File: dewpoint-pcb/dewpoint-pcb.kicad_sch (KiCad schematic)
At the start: 15 parts, among them J1 Power Terminal, J2 Relais Connector, J3 Sensor Outside, J4 Sensor Inside, J5 Display Connector, J6 Reset Button, J7 3-way On/Auto/Off-Switch

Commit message: v1.0, gerber.zip
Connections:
- net GND: now also J2.1 (Pin_1); no longer J2.3 (Pin_3)
- net Relais: now also J2.3 (Pin_3); no longer J2.1 (Pin_1)
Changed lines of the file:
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@@
     )
   )
-  (global_label "Relais" (shape input) (at 91.44 68.58 0) (fields_autoplaced)
+  (global_label "Relais" (shape input) (at 91.44 63.5 0) (fields_autoplaced)
     (effects (font (size 1.27 1.27)) (justify left))
-    (property "Intersheet References" "${INTERSHEET_REFS}" (id 0) (at 99.6588 68.6594 0)
+    (property "Intersheet References" "${INTERSHEET_REFS}" (id 0) (at 99.6588 63.5794 0)
       (effects (font (size 1.27 1.27)) (justify left) hide)
     )
@@
     (pin "1")
   )
-  (symbol (lib_id "power:GND") (at 91.44 63.5 90) (unit 1)
-    (in_bom yes) (on_board yes) (fields_autoplaced)
-    (property "Reference" "#PWR01" (id 0) (at 97.79 63.5 0)
-      (effects (font (size 1.27 1.27)) hide)
-    )
-    (property "Value" "GND" (id 1) (at 95.25 63.4999 90)
-      (effects (font (size 1.27 1.27)) (justify right))
-    )
-    (property "Footprint" "" (id 2) (at 91.44 63.5 0)
-      (effects (font (size 1.27 1.27)) hide)
-    )
-    (property "Datasheet" "" (id 3) (at 91.44 63.5 0)
-      (effects (font (size 1.27 1.27)) hide)
-    )
+  (symbol (lib_id "power:GND") (at 91.44 68.58 90) (unit 1)
+    (in_bom yes) (on_board yes) (fields_autoplaced)
+    (property "Reference" "#PWR01" (id 0) (at 97.79 68.58 0)
+      (effects (font (size 1.27 1.27)) hide)
+    )
+    (property "Value" "GND" (id 1) (at 95.25 68.5799 90)
+      (effects (font (size 1.27 1.27)) (justify right))
+    )
+    (property "Footprint" "" (id 2) (at 91.44 68.58 0)
+      (effects (font (size 1.27 1.27)) hide)
+    )
+    (property "Datasheet" "" (id 3) (at 91.44 68.58 0)
+      (effects (font (size 1.27 1.27)) hide)
+    )

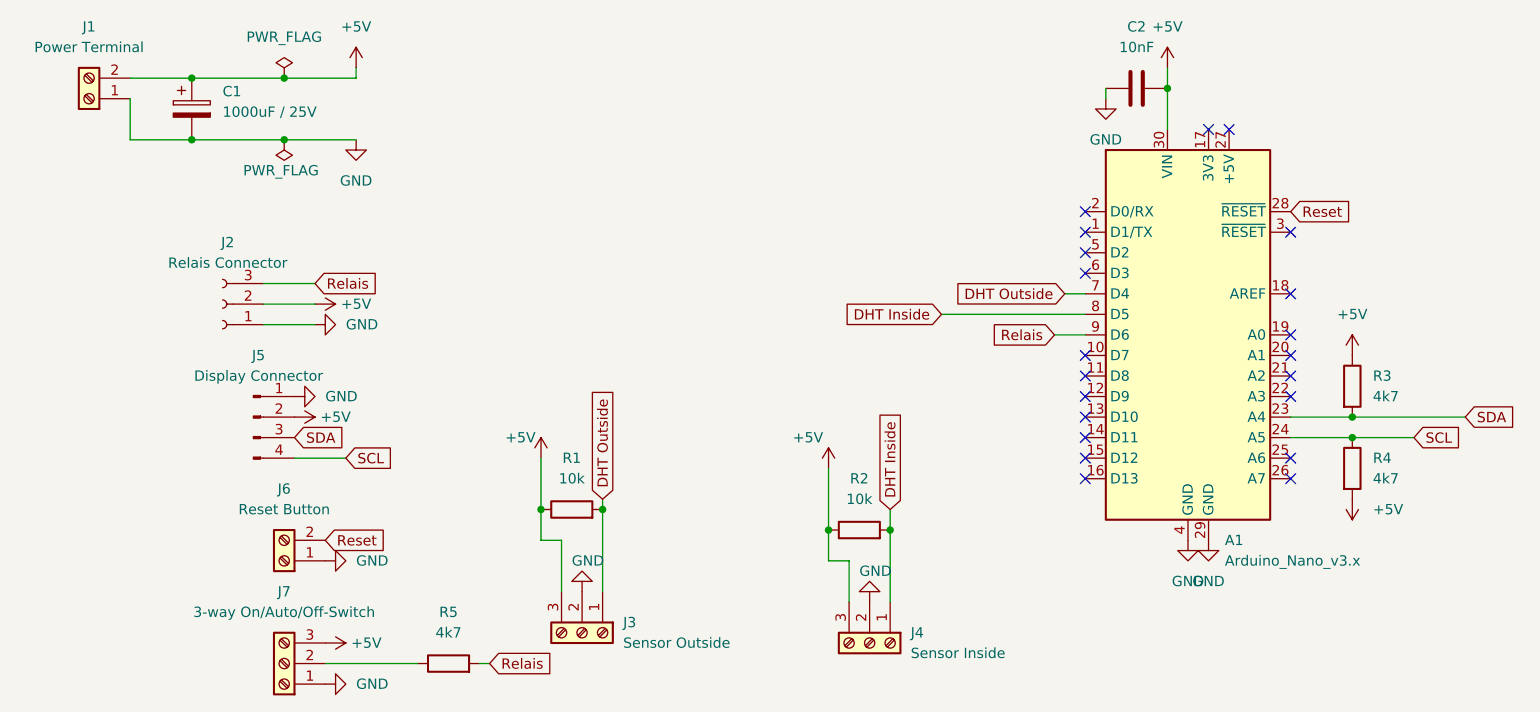
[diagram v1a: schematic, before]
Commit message: Correction, Relais switch wasn't connected correctly.
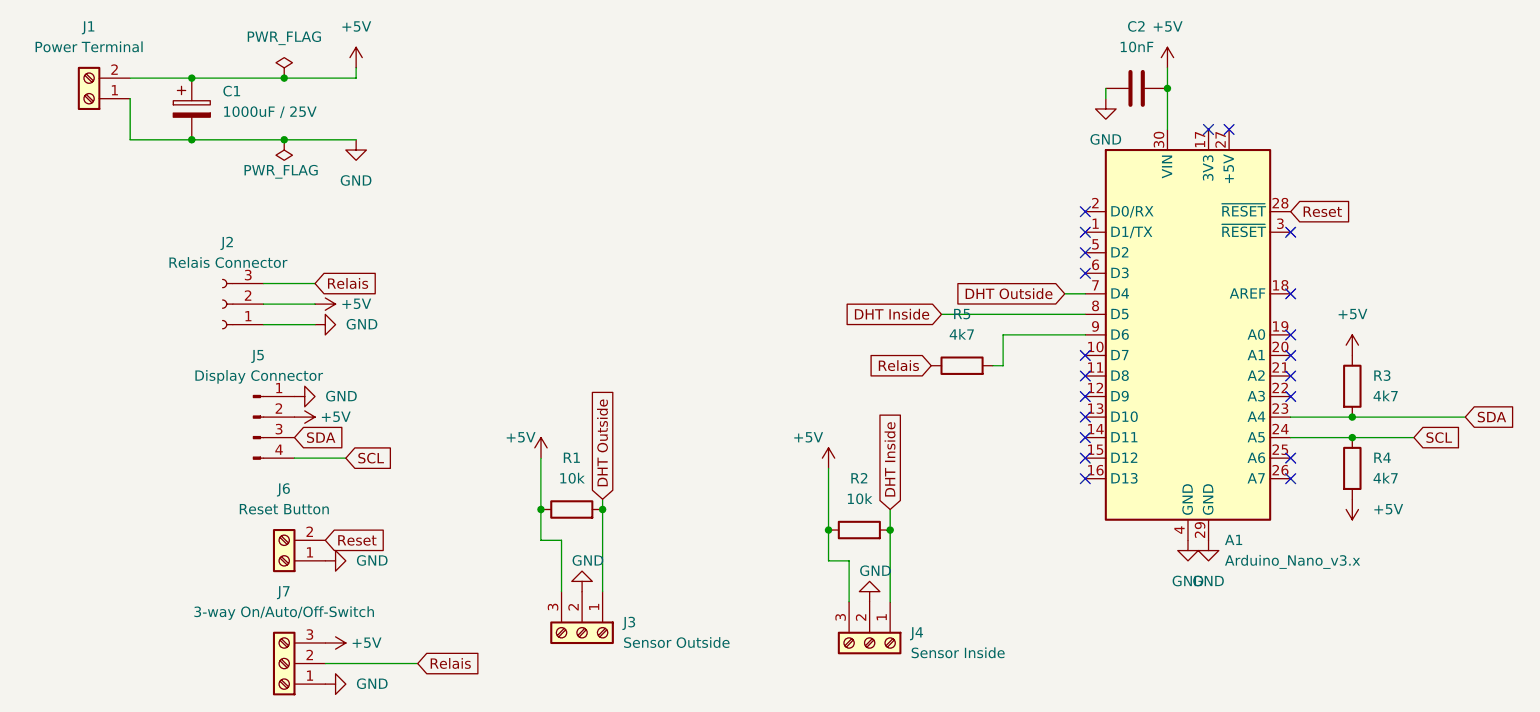
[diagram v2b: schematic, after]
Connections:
- net Relais: now also J7.2 (Pin_2), R5.1; no longer A1.9 (D6), R5.2
- new net: A1.9 (D6), R5.2
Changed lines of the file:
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@@
     (stroke (width 0) (type default) (color 0 0 0 0))
   )
-  (wire (pts (xy 182.88 69.85) (xy 186.69 69.85))
+  (wire (pts (xy 176.53 69.85) (xy 186.69 69.85))
     (stroke (width 0) (type default) (color 0 0 0 0))
   )
@@
     (stroke (width 0) (type default) (color 0 0 0 0))
   )
+  (wire (pts (xy 176.53 73.66) (xy 175.26 73.66))
+    (stroke (width 0) (type default) (color 0 0 0 0))
+  )
   (wire (pts (xy 212.09 82.55) (xy 219.71 82.55))
     (stroke (width 0) (type default) (color 0 0 0 0))
   )
-  (wire (pts (xy 111.76 110.49) (xy 113.03 110.49))
+  (wire (pts (xy 176.53 69.85) (xy 176.53 73.66))
     (stroke (width 0) (type default) (color 0 0 0 0))
   )
@@
     )
   )
-  (global_label "Relais" (shape input) (at 182.88 69.85 180) (fields_autoplaced)
+  (global_label "Relais" (shape input) (at 167.64 73.66 180) (fields_autoplaced)
     (effects (font (size 1.27 1.27)) (justify right))
-    (property "Intersheet References" "${INTERSHEET_REFS}" (id 0) (at 174.6612 69.7706 0)
+    (property "Intersheet References" "${INTERSHEET_REFS}" (id 0) (at 159.4212 73.5806 0)
       (effects (font (size 1.27 1.27)) (justify right) hide)
     )
@@
     )
   )
-  (global_label "Relais" (shape input) (at 113.03 110.49 0) (fields_autoplaced)
-    (effects (font (size 1.27 1.27)) (justify left))
-    (property "Intersheet References" "${INTERSHEET_REFS}" (id 0) (at 121.2488 110.5694 0)
+  (global_label "Relais" (shape input) (at 104.14 110.49 0) (fields_autoplaced)
+    (effects (font (size 1.27 1.27)) (justify left))
+    (property "Intersheet References" "${INTERSHEET_REFS}" (id 0) (at 112.3588 110.5694 0)
       (effects (font (size 1.27 1.27)) (justify left) hide)
     )
@@
     (pin "3")
   )
-  (symbol (lib_id "Device:R") (at 107.95 110.49 90) (unit 1)
-    (in_bom yes) (on_board yes) (fields_autoplaced)
-    (property "Reference" "R5" (id 0) (at 107.95 104.14 90))
-    (property "Value" "4k7" (id 1) (at 107.95 106.68 90))
-    (property "Footprint" "Resistor_THT:R_Axial_DIN0207_L6.3mm_D2.5mm_P10.16mm_Horizontal" (id 2) (at 107.95 112.268 90)
-      (effects (font (size 1.27 1.27)) hide)
-    )
-    (property "Datasheet" "~" (id 3) (at 107.95 110.49 0)
-      (effects (font (size 1.27 1.27)) hide)
-    )
-    (pin "1")
-    (pin "2")
-  )
   (symbol (lib_id "power:GND") (at 199.39 95.25 0) (unit 1)
     (in_bom yes) (on_board yes) (fields_autoplaced)
@@
     )
     (pin "1")
+  )
+  (symbol (lib_id "Device:R") (at 171.45 73.66 90) (unit 1)
+    (in_bom yes) (on_board yes) (fields_autoplaced)
+    (property "Reference" "R5" (id 0) (at 171.45 67.31 90))
+    (property "Value" "4k7" (id 1) (at 171.45 69.85 90))
+    (property "Footprint" "Resistor_THT:R_Axial_DIN0207_L6.3mm_D2.5mm_P10.16mm_Horizontal" (id 2) (at 171.45 75.438 90)
+      (effects (font (size 1.27 1.27)) hide)
+    )
+    (property "Datasheet" "~" (id 3) (at 171.45 73.66 0)
+      (effects (font (size 1.27 1.27)) hide)
+    )
+    (pin "1")
+    (pin "2")
   )
   (symbol (lib_id "Connector:Screw_Terminal_01x02") (at 87.63 97.79 180) (unit 1)
@@
       (reference "R4") (unit 1) (value "4k7") (footprint "Resistor_THT:R_Axial_DIN0207_L6.3mm_D2.5mm_P10.16mm_Horizontal")
     )
-    (path "/735f57e2-2778-47b2-b14a-8899a681a653"
+    (path "/95804866-6482-4774-aadd-4d9c6ecc7eb8"
       (reference "R5") (unit 1) (value "4k7") (footprint "Resistor_THT:R_Axial_DIN0207_L6.3mm_D2.5mm_P10.16mm_Horizontal")
     )
